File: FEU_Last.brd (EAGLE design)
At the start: 72.3 x 62.8 mm, 67 parts, among them IC1 LM358N, IC3 FT232RL, Q1 8M, Q2 32748, X2 MINI-USB-32005-201

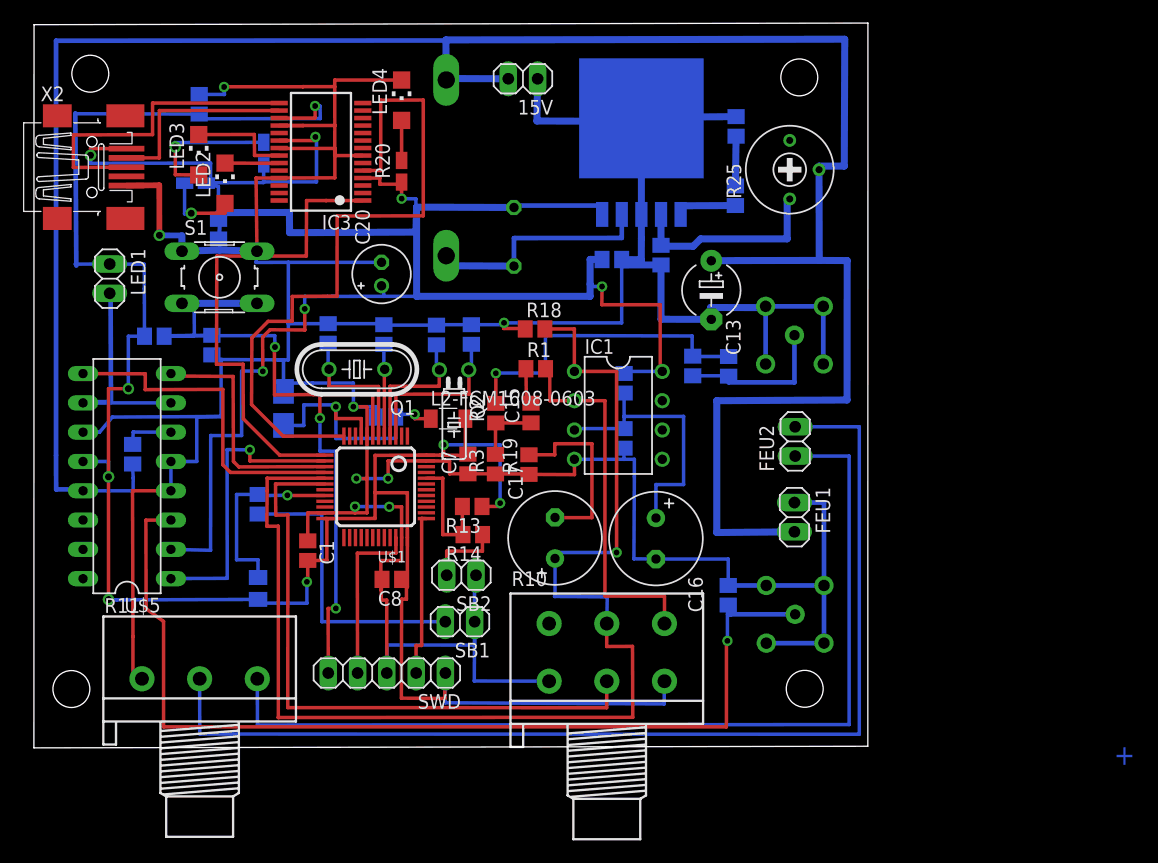
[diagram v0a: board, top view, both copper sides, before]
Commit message: Factory board with FT232- 2
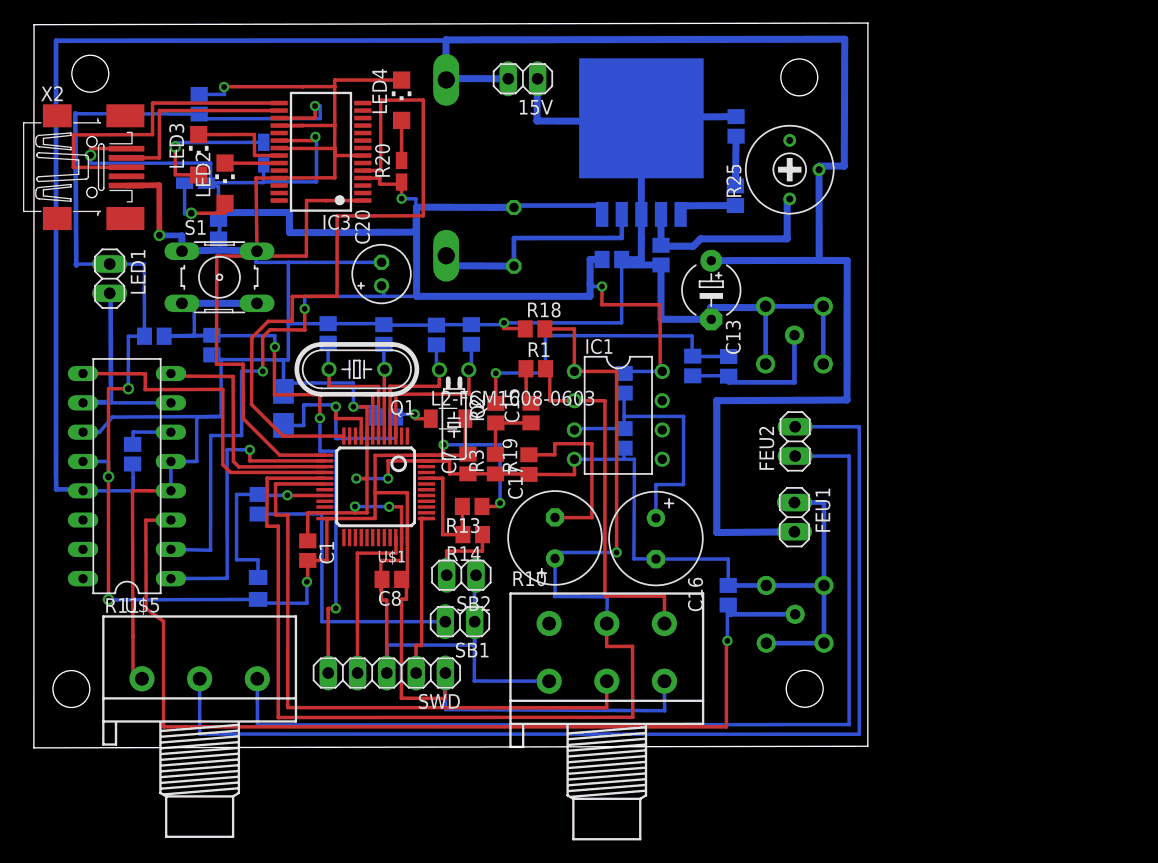
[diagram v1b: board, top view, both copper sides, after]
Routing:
- net 3.3V: track 196.3 -> 197.5 mm
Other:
- board text removed: "+"
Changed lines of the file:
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@@
 <board>
 <plain>
-<text x="9.13" y="53.21" size="1.778" layer="16" rot="MR0">+</text>
-<text x="95.46" y="6.83" size="1.778" layer="16" rot="MR0">+</text>
 <wire x1="0" y1="71" x2="72.3" y2="71.14" width="0" layer="20"/>
 <wire x1="72.3" y1="71.14" x2="72.29" y2="8.44" width="0" layer="20"/>
@@
 <wire x1="35.62" y1="12.58" x2="35.62" y2="14.65" width="0.3048" layer="1"/>
 <wire x1="35.62" y1="14.65" x2="35.67" y2="14.79" width="0.3048" layer="1"/>
-<wire x1="35.67" y1="14.79" x2="35.65" y2="12.21" width="0.3048" layer="16"/>
-<wire x1="35.65" y1="12.21" x2="54.64" y2="12.11" width="0.3048" layer="16"/>
-<wire x1="54.64" y1="12.11" x2="54.64" y2="14.25" width="0.3048" layer="16"/>
+<wire x1="35.67" y1="14.79" x2="35.69" y2="11.62" width="0.3048" layer="16"/>
+<wire x1="35.69" y1="11.62" x2="54.68" y2="11.52" width="0.3048" layer="16"/>
+<wire x1="54.68" y1="11.52" x2="54.64" y2="14.25" width="0.3048" layer="16"/>
 <wire x1="54.64" y1="14.25" x2="54.66" y2="14.08" width="0.3048" layer="16"/>
 <wire x1="19.42" y1="21.17" x2="19.637946875" y2="20.889175" width="0.3048" layer="16"/>

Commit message: Factory board with FT232- 3
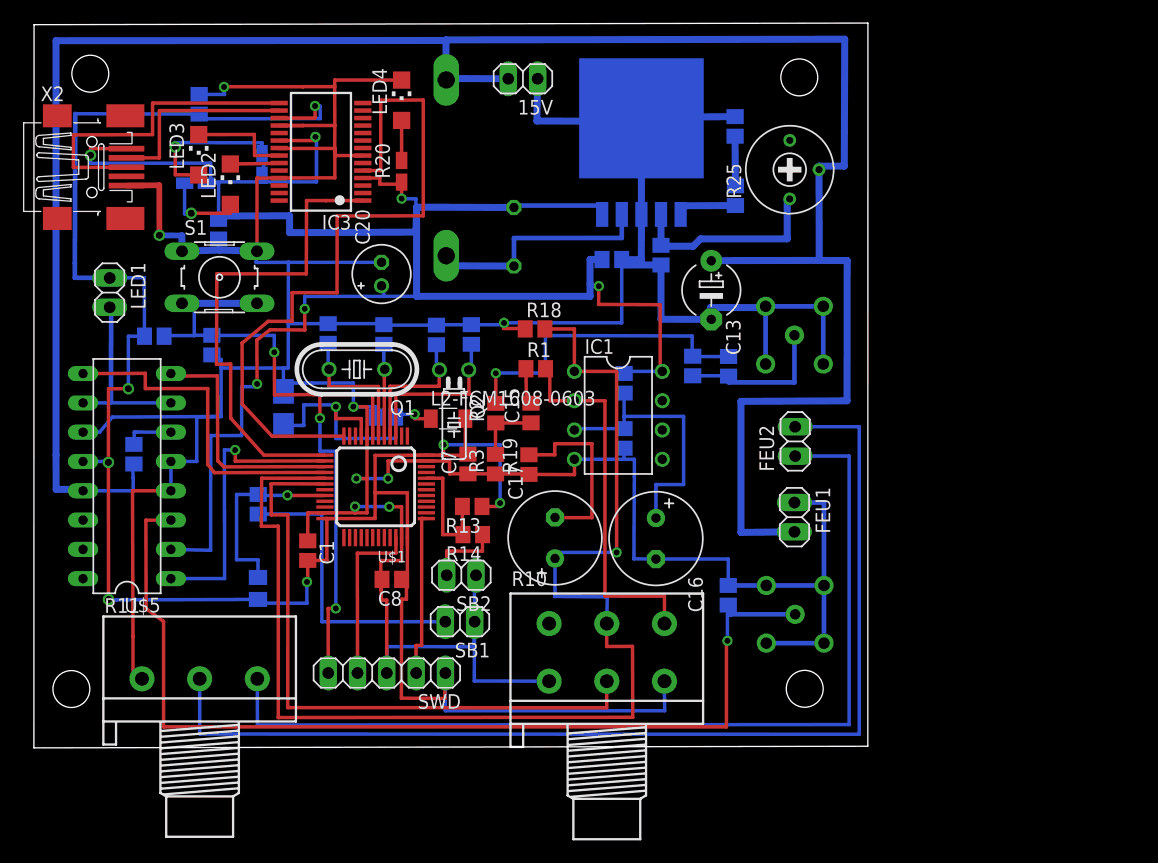
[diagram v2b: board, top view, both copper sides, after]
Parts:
- moved LED1 1.21 mm to (6.56, 47.8)
- moved R17 0.99 mm to (19.8, 58.9)
- moved LED2 0.47 mm to (17.0, 57.2)
- moved R4 0.11 mm to (8.66, 33.8)
- moved C11 0.09 mm to (60.8, 62.2)
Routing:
- net NRST: track 75.1 -> 68.7 mm
- net 15V: track 203.3 -> 199.2 mm
- net GND: track 420.2 -> 416.1 mm
- net N$4: track 19.9 -> 16.1 mm
- net 3.3V: track 197.5 -> 196.1 mm
- net USART_TX_STM: track 60.9 -> 62.2 mm
- net ADC_S: track 109.6 -> 110.6 mm
- net N$21: track 12.6 -> 13.4 mm
- net ADC_RES: track 54.7 -> 55.5 mm
- net USB+: track 176.2 -> 175.5 mm

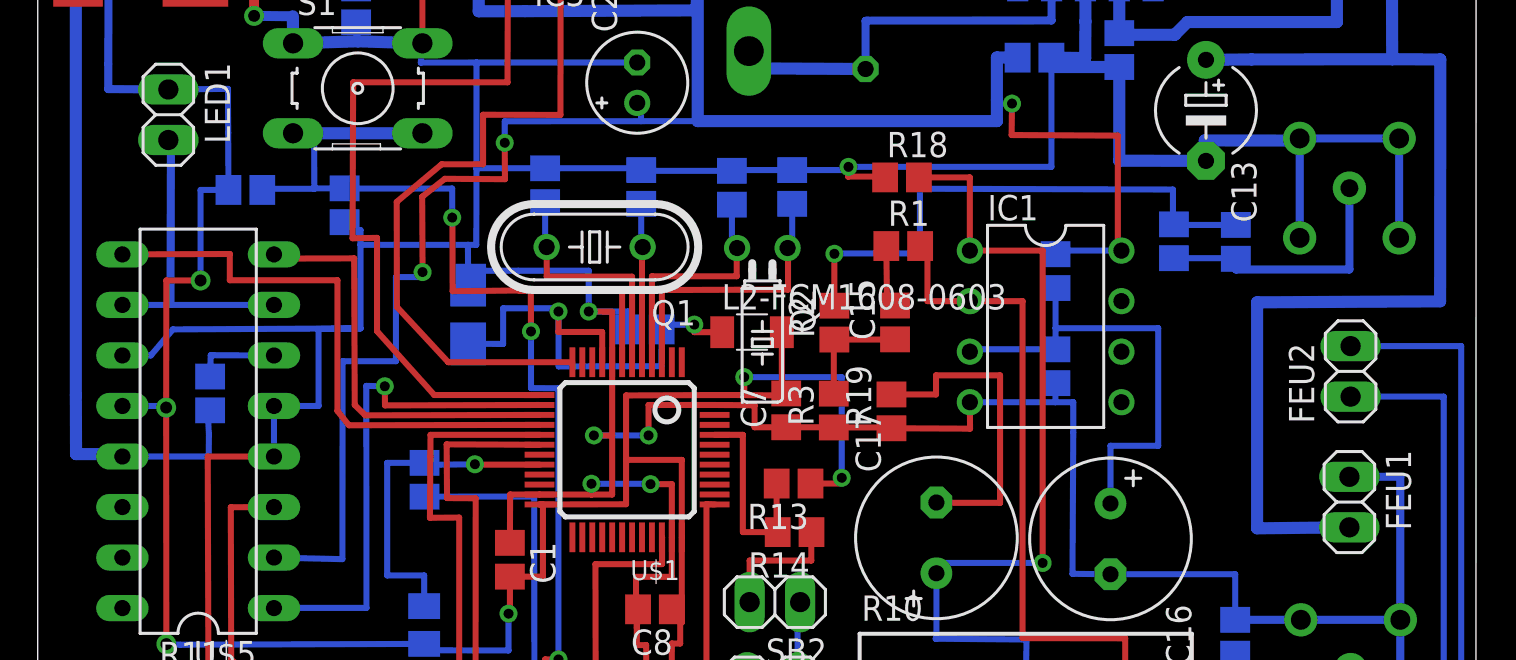
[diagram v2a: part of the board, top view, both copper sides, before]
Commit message: Add current-to voltage converter
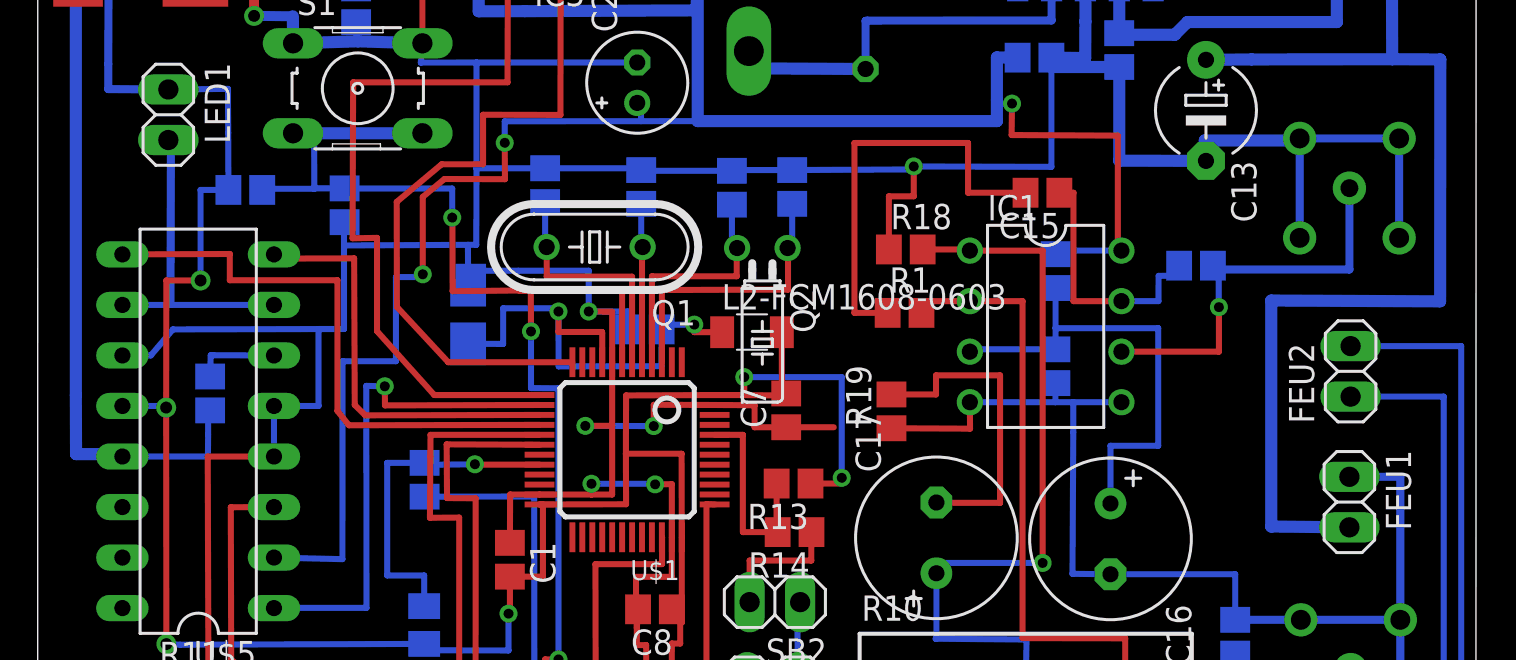
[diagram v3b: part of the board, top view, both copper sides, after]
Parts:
- removed C14: 15p, resistor:C0805
- removed R3: 2.7k, resistor:R0805
- removed R9: 1M, resistor:R0805
- R2: value 10k -> 27k
- moved R2 18.4 mm to (58.2, 40.2), flipped to the bottom, turned to 0 degrees
- moved C15 9.87 mm to (50.5, 43.9), turned to 180 degrees
- moved R18 3.62 mm to (43.6, 41.0)
- moved R1 3.36 mm to (43.6, 37.8)
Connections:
- removed net N$8: C14.2, R2.2, R9.1
- net GND: now also IC1.5; no longer R3.1
- net N$6: now also IC1.6, U$2.ATN; no longer C15.1, R3.2
- net N$7: now also C15.1, IC1.7, R2.2; no longer C14.1, R9.2, U$2.ATN
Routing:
- net N$8: track 27.8 -> 0.00 mm, vias 1 -> 0
- net N$9: track 3.39 -> 21.3 mm
- net N$6: track 5.81 -> 20.2 mm, vias 0 -> 1
- net ADC_S: track 110.6 -> 106.8 mm
- net N$11: track 32.4 -> 29.9 mm
- net GND: track 416.1 -> 417.7 mm
- net 15V: track 199.2 -> 197.7 mm
